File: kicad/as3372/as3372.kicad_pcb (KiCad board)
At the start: 4 copper layers, 80 x 80 mm, 164 parts, among them J1 Conn_01x01, J2 Conn_01x02, J3 Conn_02x20_Odd_Even, Q1 MMBT3904, Q2 MMBT3904, U1 MUX508, U10 TL072, U11 DG442xY, U13 LM4040AIM3-2.5, U15 M24C02-WMN, U17 MUX508, U18 NE5532, U19 L79L05_TO92, U2 MUX508, U3 NE5532, U4 TL074, U5 TL072, U6 TL074, U7 CAT9555YI-T2, U8 AS3372, U9 AD5328

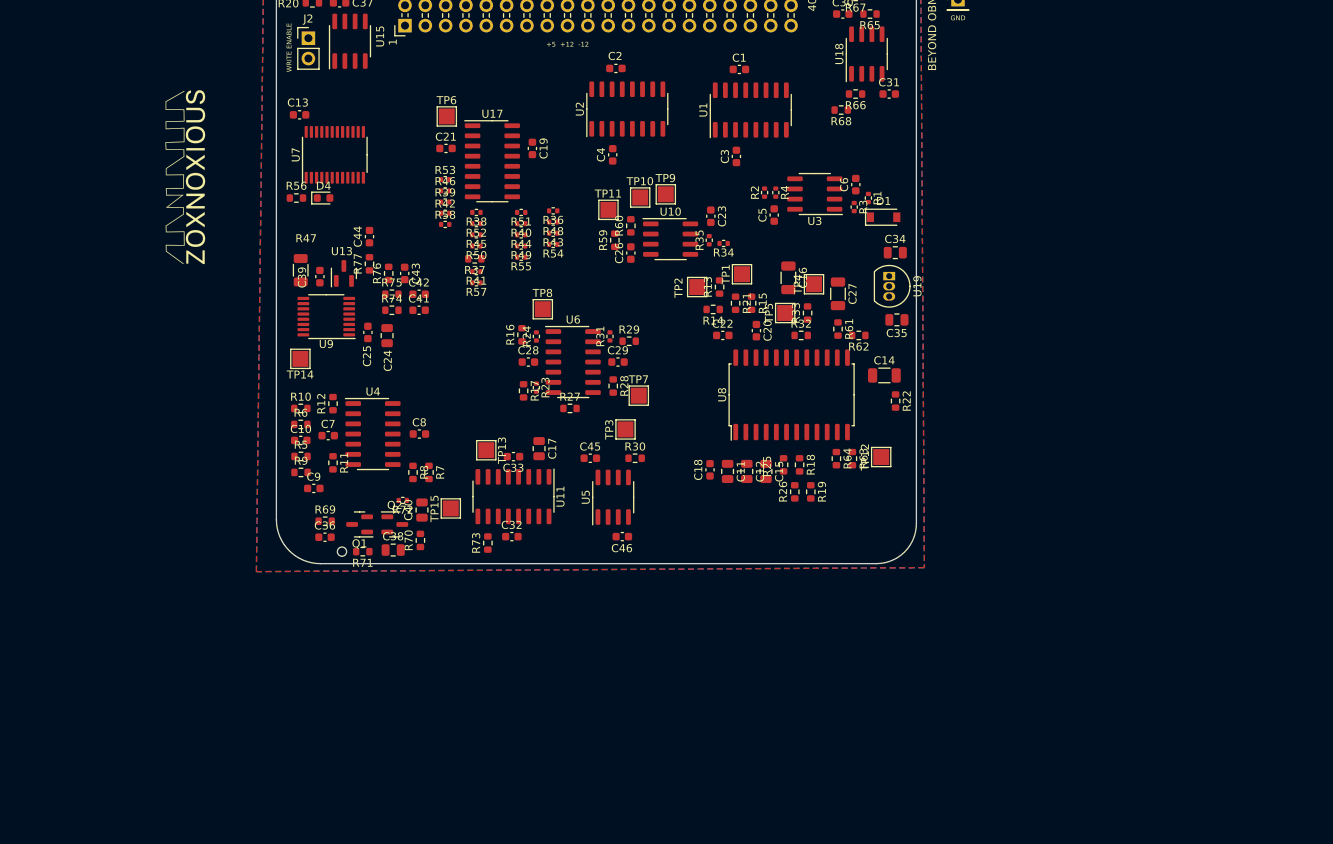
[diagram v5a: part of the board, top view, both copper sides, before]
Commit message: having a tough time routing full filter with modes
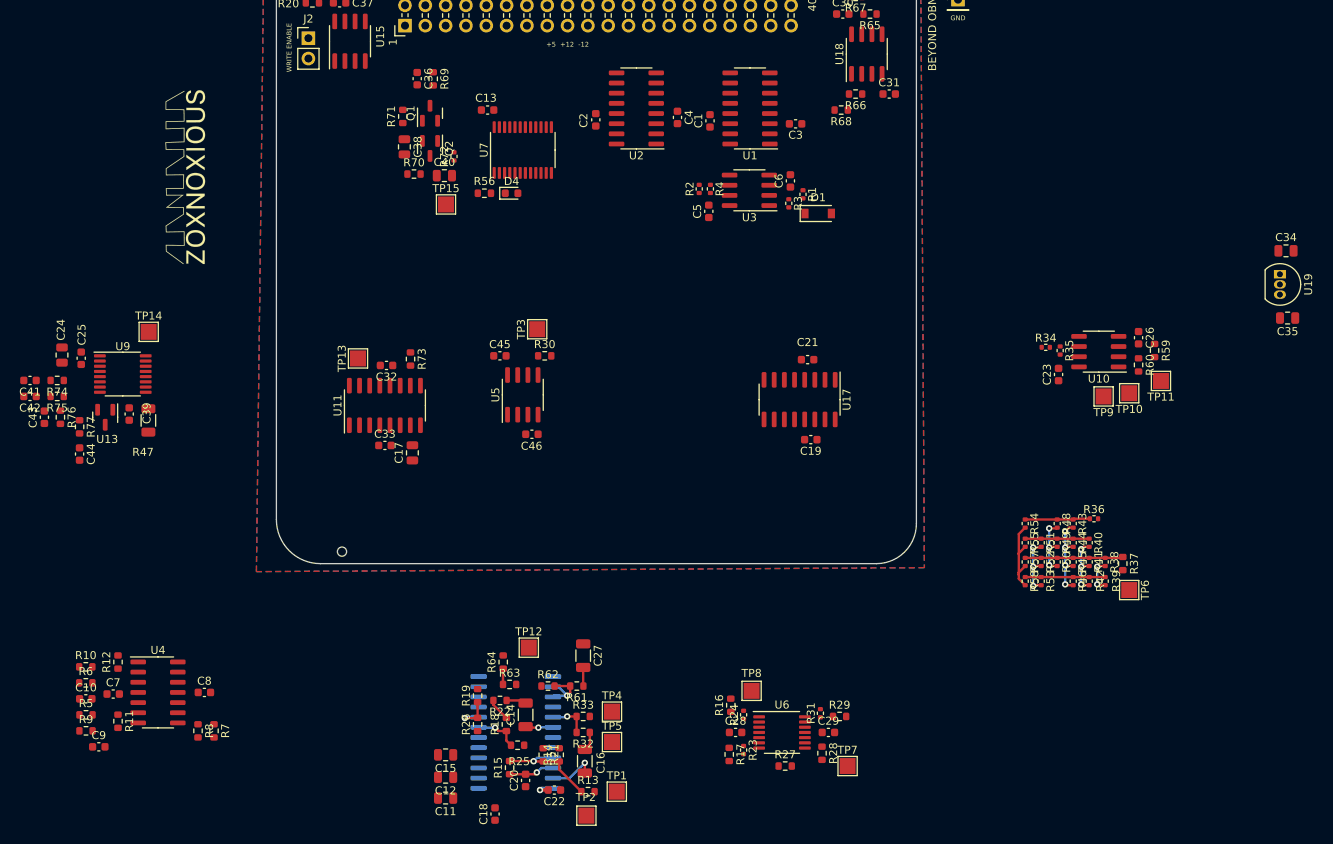
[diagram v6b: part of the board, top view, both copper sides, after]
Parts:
- U6: footprint Package_SO:SOIC-14_3.9x8.7mm_P1.27mm -> Package_SO:TSSOP-14_4.4x5mm_P0.65mm
- U8: moved to B.Cu
- moved TP6 103.8 mm to (173.6, 108.8), turned to -90 degrees
- moved R39 95.1 mm to (170.6, 107.7), turned to -90 degrees
- moved R42 92.7 mm to (168.6, 107.7), turned to -90 degrees
- moved R46 92.4 mm to (166.6, 107.7), turned to -90 degrees
- moved R38 89.9 mm to (170.6, 105.3), turned to -90 degrees
- moved R53 89.8 mm to (162.6, 107.7), turned to -90 degrees
- moved R37 89.5 mm to (172.8, 105.5), turned to -90 degrees
- moved R58 85.1 mm to (160.6, 107.7), turned to -90 degrees
- moved R45 85.1 mm to (166.6, 105.3), turned to -90 degrees
- moved R41 84.8 mm to (168.6, 105.3), turned to -90 degrees
- moved R50 82.6 mm to (164.6, 105.3), turned to -90 degrees
- moved R52 82.3 mm to (162.6, 105.3), turned to -90 degrees
- moved R40 81.4 mm to (168.6, 102.9), turned to -90 degrees
- moved R44 79.0 mm to (166.6, 102.9), turned to -90 degrees
- moved R36 77.8 mm to (169.2, 99.9), turned to 0 degrees
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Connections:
- U1 pad 10: /CARD6_OUT2 -> /CARD1_OUT2
- U1 pad 11: /CARD5_OUT1 -> /CARD2_OUT2
- U1 pad 12: /CARD4_OUT2 -> /CARD3_OUT1
- U1 pad 4: /CARD1_OUT1 -> /CARD7_OUT1
- U1 pad 5: /CARD1_OUT2 -> /CARD6_OUT2
- U1 pad 6: /CARD2_OUT2 -> /CARD5_OUT1
- U1 pad 7: /CARD3_OUT1 -> /CARD4_OUT2
- U1 pad 9: /CARD7_OUT1 -> /CARD1_OUT1
- U11 pad 1: /FILTER_D_CTRL -> /VCF_FM_CTRL
- U11 pad 15: /filter_as3372/VCF_FM -> /filter_as3372/VCA_FM
- U11 pad 16: /VCF_FM_CTRL -> /VCA_FM_CTRL
- U11 pad 2: Net-(C17-Pad2) -> /filter_as3372/VCF_FM
- U11 pad 3: Net-(C18-Pad2) -> Net-(U11-Pad3)
- U11 pad 6: /filter_as3372/VCA_FM -> Net-(C17-Pad2)
- U11 pad 7: Net-(U11-Pad7) -> Net-(C18-Pad2)
- U11 pad 8: /VCA_FM_CTRL -> /FILTER_D_CTRL
- U2 pad 10: /CARD6_OUT1 -> /CARD1_OUT2
- U2 pad 11: /CARD5_OUT2 -> /CARD2_OUT1
- U2 pad 12: /CARD4_OUT1 -> /CARD2_OUT2
- U2 pad 4: /CARD1_OUT2 -> /CARD6_OUT1
- U2 pad 5: /CARD2_OUT1 -> /CARD5_OUT2
- U2 pad 6: /CARD2_OUT2 -> /CARD4_OUT1
- U2 pad 9: /CARD7_OUT1 -> unconnected-(U2-Pad9)
- U5 pad 1: Net-(U11-Pad7) -> Net-(U11-Pad14)
- U5 pad 2: Net-(U11-Pad7) -> Net-(U11-Pad14)
- U5 pad 6: Net-(U11-Pad14) -> Net-(U11-Pad3)
- U5 pad 7: Net-(U11-Pad14) -> Net-(U11-Pad3)
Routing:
- net Net-(R13-Pad1): track 0.00 -> 13.7 mm, vias 0 -> 1
- net /filter_as3372/CELL2_BUFFERED: track 0.00 -> 12.2 mm
- net /filter_as3372/3PHP_OR_3PHP_1PLP: track 0.00 -> 10.9 mm, vias 0 -> 4
- net /filter_as3372/3PAP_OR_3PAP_1PLP: track 0.00 -> 10.5 mm
- net /filter_as3372/CELL1_BUFFERED: track 0.00 -> 10.0 mm
- net /filter_as3372/VCF_OUT_BUFFERED: track 0.00 -> 8.13 mm
- net /filter_as3372/CELL3_BUFFERED: track 0.00 -> 8.00 mm
- net /filter_as3372/2PN_OR_2PN_1PLP: track 0.00 -> 7.91 mm, vias 0 -> 3
- net /filter_as3372/2PHP_1PLP_OR_4PBP: track 0.00 -> 7.72 mm, vias 0 -> 3
- net /filter_as3372/2PHP_OR_2PHP_1PLP: track 0.00 -> 7.60 mm, vias 0 -> 3
- net Net-(R61-Pad2): track 0.00 -> 7.38 mm, vias 0 -> 1
- net Net-(C16-Pad1): track 0.00 -> 6.04 mm, vias 0 -> 1
- net -5V: track 0.00 -> 5.75 mm, vias 0 -> 1
- net Net-(R18-Pad1): track 0.00 -> 5.68 mm, vias 0 -> 1
- net Net-(R19-Pad1): track 0.00 -> 5.33 mm, vias 0 -> 1
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- removed copper zone on In2.Cu, net +5V

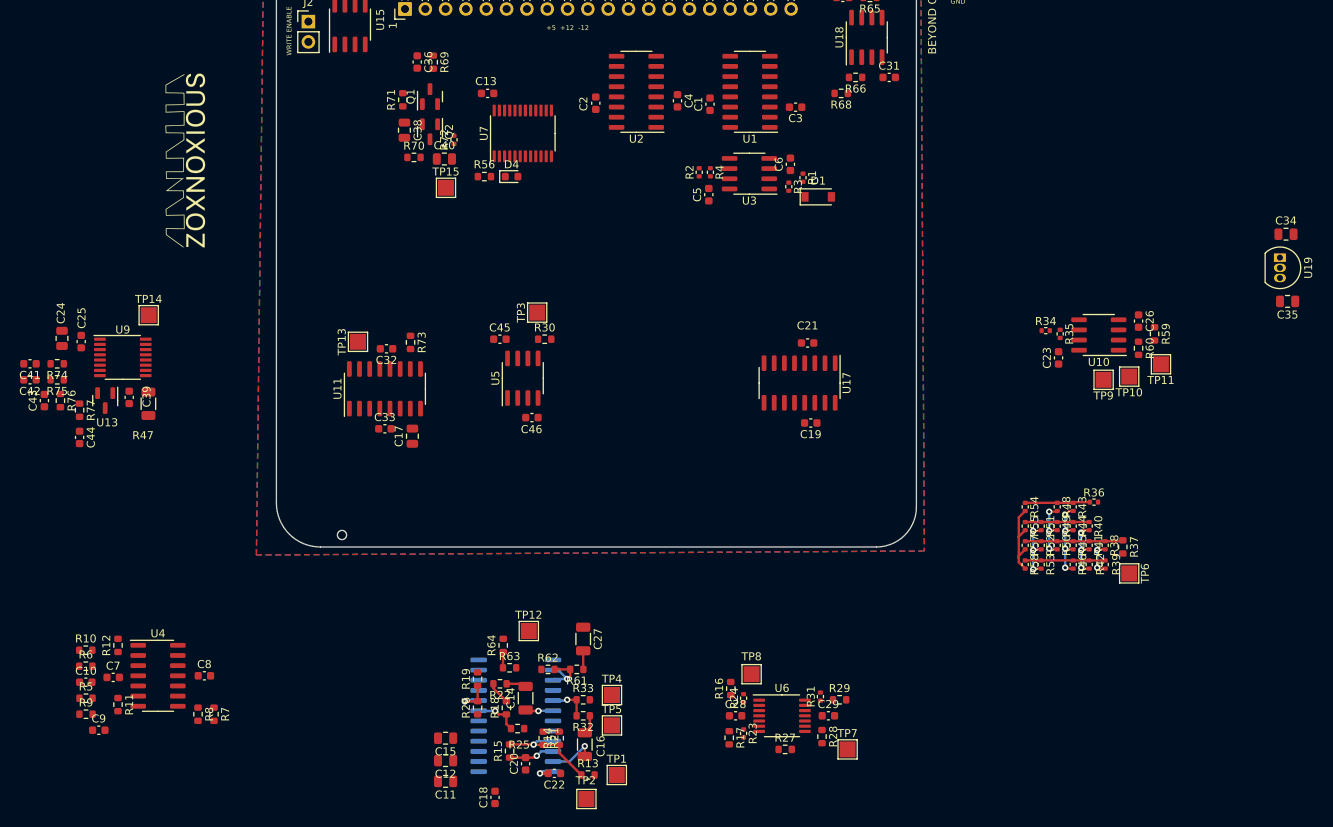
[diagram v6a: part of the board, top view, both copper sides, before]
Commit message: simplify and remove filter mode select
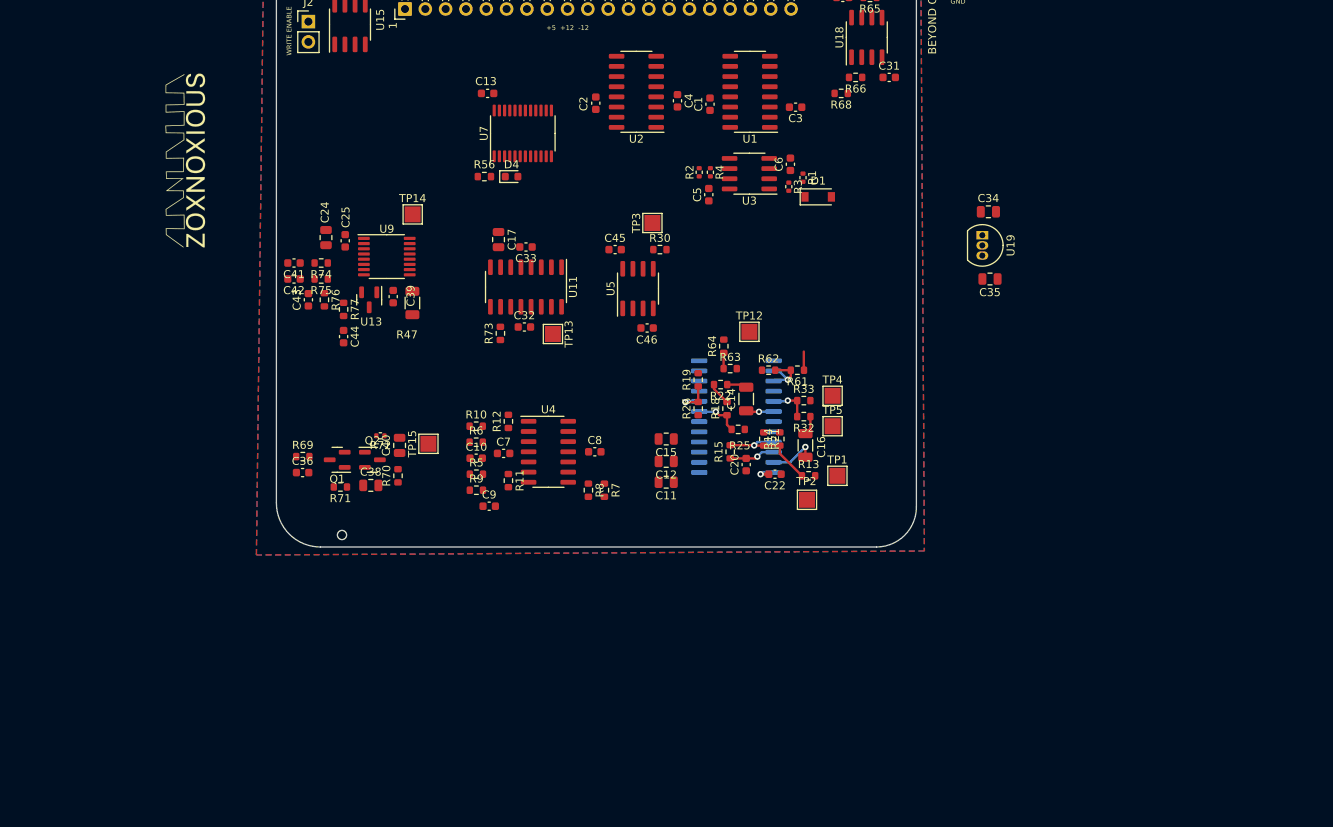
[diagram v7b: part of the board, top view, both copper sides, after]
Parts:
- removed C18: 33p, Capacitor_SMD:C_0603_1608Metric
- removed C19, C21, C23, C26, C28, C29: 0.1u, Capacitor_SMD:C_0603_1608Metric
- removed C27: 2.2u, Capacitor_SMD:C_1206_3216Metric
- removed R16, R17, R29: 1k, Resistor_SMD:R_0603_1608Metric
- removed R23, R24, R31, R34, R35, R38, R39, R40, R42, R43, R46, R48, R50, R53, R58: 100k, Resistor_SMD:R_0402_1005Metric
- removed R27, R28, R59: 10k, Resistor_SMD:R_0603_1608Metric
- removed R36: 56k, Resistor_SMD:R_0402_1005Metric
- removed R37: 62k, Resistor_SMD:R_0603_1608Metric
- removed R41, R49, R51, R52: 49.9k, Resistor_SMD:R_0402_1005Metric
- removed R44, R45, R57: 33.2k, Resistor_SMD:R_0402_1005Metric
- removed R54: 24.9k, Resistor_SMD:R_0402_1005Metric
- removed R55: 16.5k, Resistor_SMD:R_0402_1005Metric
- removed R60: 68k, Resistor_SMD:R_0603_1608Metric
- removed TP10, TP11, TP6, TP7, TP8, TP9: TestPoint, TestPoint:TestPoint_Pad_2.0x2.0mm
- removed U10: TL072, Package_SO:SOIC-8_3.9x4.9mm_P1.27mm
- removed U17: MUX508, Package_SO:SOIC-16_3.9x9.9mm_P1.27mm
- removed U6: TL074, Package_SO:TSSOP-14_4.4x5mm_P0.65mm
- moved C10 56.3 mm to (92.0, 94.4)
- moved C7 56.3 mm to (95.4, 93.8)
- moved C8 56.3 mm to (106.8, 93.6)
- moved C9 56.3 mm to (93.6, 100.4)
- moved R10 56.3 mm to (92.0, 90.4)
- moved R11 56.3 mm to (96.0, 97.2)
- moved R12 56.3 mm to (96.0, 89.8)
- moved R5 56.3 mm to (92.0, 96.4)
- moved R6 56.3 mm to (92.0, 92.4)
- moved R7 56.3 mm to (108.0, 98.4)
- moved R8 56.3 mm to (106.0, 98.4)
- moved R9 56.3 mm to (92.0, 98.4)
- moved U4 56.3 mm to (101.0, 93.6)
- moved C36 53.3 mm to (70.3, 96.2), turned to 0 degrees
- moved R69 51.9 mm to (70.3, 94.2), turned to 0 degrees
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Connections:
- C17 pad 2: Net-(C17-Pad2) -> Net-(U8-Pad1)
- R61 pad 1: Net-(C27-Pad2) -> Net-(C16-Pad2)
- U11 pad 6: Net-(C17-Pad2) -> (no net)
- U11 pad 7: Net-(C18-Pad2) -> (no net)
- U11 pad 8: /FILTER_D_CTRL -> (no net)
- U7 pad 6: /FILTER_A_CTRL -> unconnected-(U7-Pad6)
- U7 pad 7: /FILTER_B_CTRL -> unconnected-(U7-Pad7)
- U7 pad 8: /FILTER_C_CTRL -> unconnected-(U7-Pad8)
- U7 pad 9: /FILTER_D_CTRL -> unconnected-(U7-Pad9)
- U8 pad 1: Net-(C18-Pad2) -> Net-(U8-Pad1)
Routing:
- net /filter_as3372/CELL2_BUFFERED: track 12.2 -> 0.00 mm
- net /filter_as3372/3PHP_OR_3PHP_1PLP: track 10.9 -> 0.00 mm, vias 4 -> 0
- net /filter_as3372/3PAP_OR_3PAP_1PLP: track 10.5 -> 0.00 mm
- net /filter_as3372/CELL1_BUFFERED: track 10.0 -> 0.00 mm
- net /filter_as3372/VCF_OUT_BUFFERED: track 8.13 -> 0.00 mm
- net /filter_as3372/CELL3_BUFFERED: track 8.00 -> 0.00 mm
- net /filter_as3372/2PN_OR_2PN_1PLP: track 7.91 -> 0.00 mm, vias 3 -> 0
- net /filter_as3372/2PHP_1PLP_OR_4PBP: track 7.72 -> 0.00 mm, vias 3 -> 0
- net /filter_as3372/2PHP_OR_2PHP_1PLP: track 7.60 -> 0.00 mm, vias 3 -> 0
- net /filter_as3372/1PLP_OR_2PBP: track 4.28 -> 0.00 mm, vias 2 -> 0
- net Net-(C27-Pad2): track 2.34 -> 0.00 mm
- net Net-(C16-Pad2): track 2.63 -> 4.97 mm

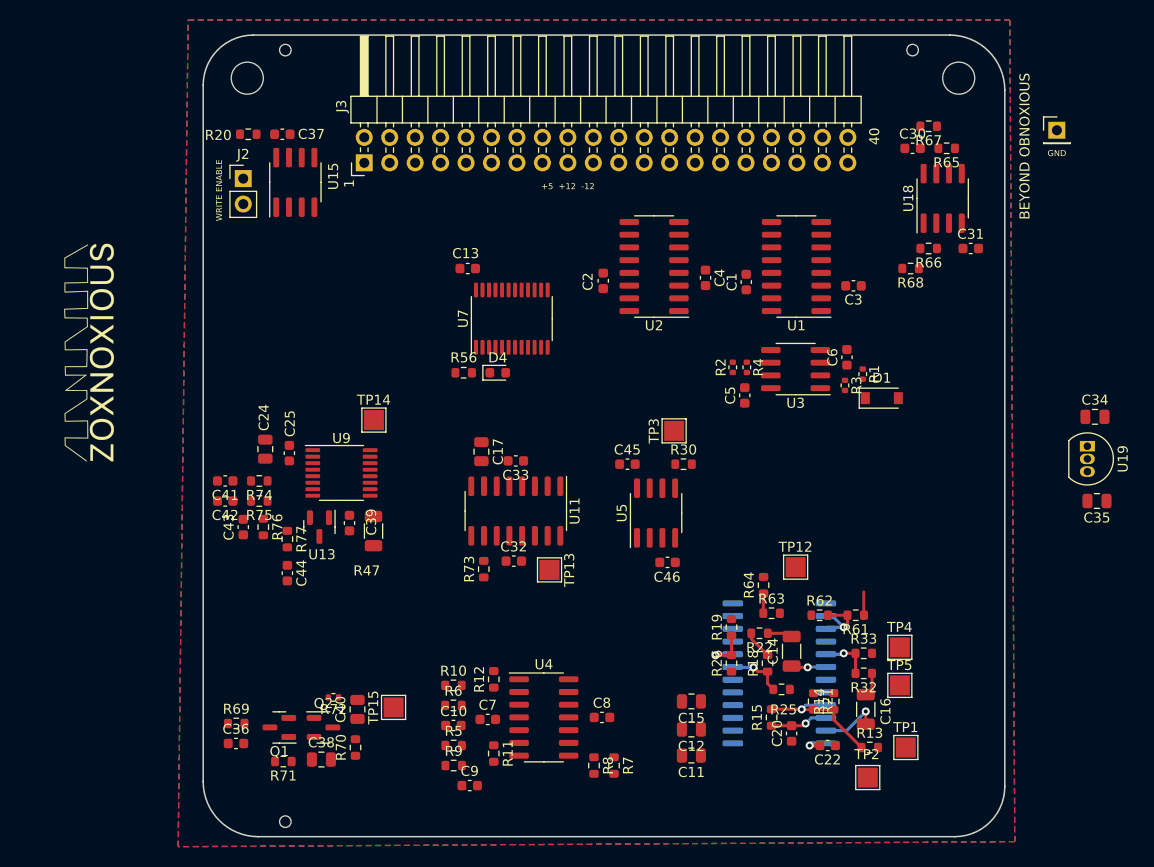
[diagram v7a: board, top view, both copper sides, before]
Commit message: starting routing...which may be detrimental
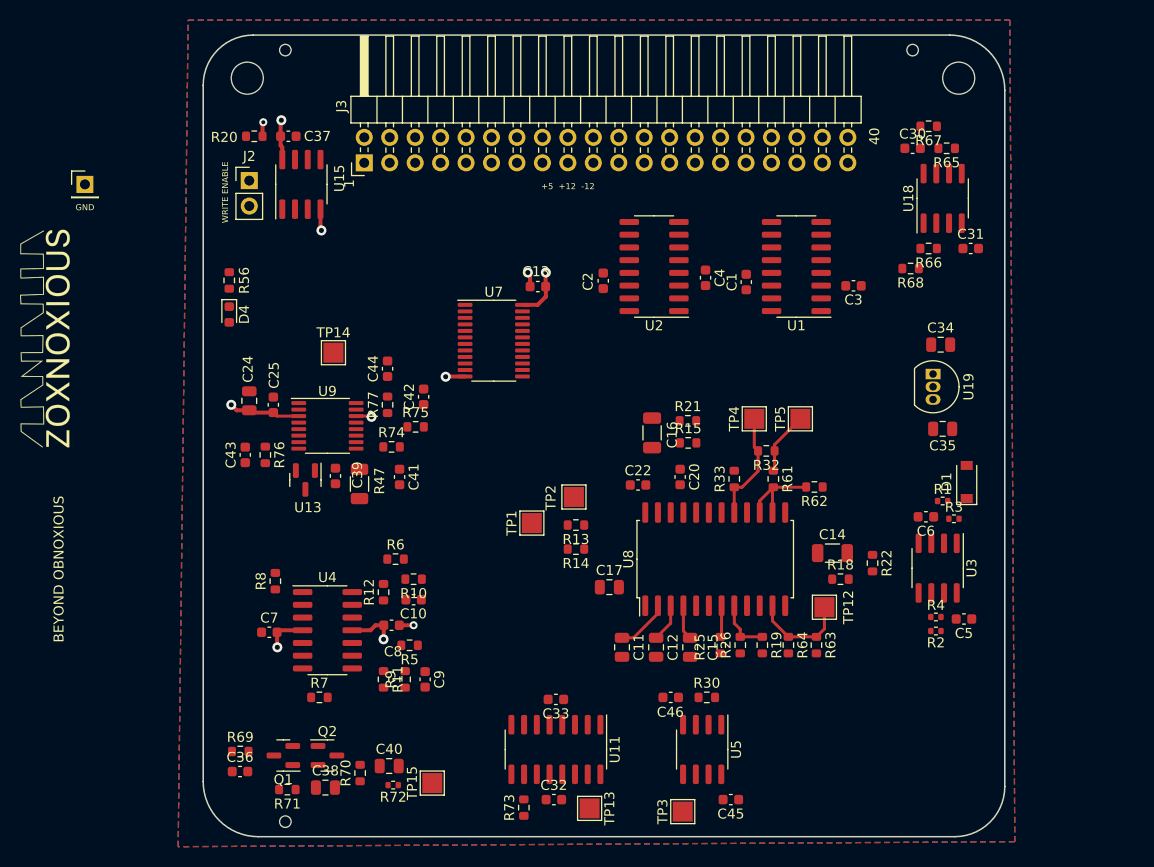
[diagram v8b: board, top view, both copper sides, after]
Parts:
- R61: value 47k -> 22k
- U8: moved to F.Cu
- moved J1 97.2 mm to (55.2, 40.4)
- moved TP1 43.5 mm to (99.8, 74.2), turned to 90 degrees
- moved TP2 40.5 mm to (104.0, 71.6), turned to 90 degrees
- moved TP3 38.0 mm to (114.9, 103.0)
- moved R13 36.8 mm to (104.2, 74.4), turned to 180 degrees
- moved R8 36.7 mm to (74.2, 80.0), turned to 90 degrees
- moved C45 35.0 mm to (119.7, 101.8), turned to 180 degrees
- moved C16 34.9 mm to (111.8, 65.2)
- moved R2 33.2 mm to (140.1, 85.0), turned to 180 degrees
- moved C22 32.2 mm to (110.4, 70.4), turned to 0 degrees
- moved R4 31.3 mm to (140.1, 83.6), turned to 0 degrees
- moved C5 31.2 mm to (142.9, 83.8), turned to 180 degrees
- moved R21 30.7 mm to (115.4, 64.0), turned to 0 degrees
- moved R7 30.2 mm to (78.6, 91.6), turned to 0 degrees
- moved R14 29.9 mm to (104.2, 76.8), turned to 180 degrees
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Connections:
- U11 pad 14: Net-(U11-Pad14) -> /filter_as3372/VCA_FM
- U11 pad 15: /filter_as3372/VCA_FM -> Net-(U11-Pad15)
- U11 pad 2: /filter_as3372/VCF_FM -> Net-(U11-Pad2)
- U11 pad 3: Net-(U11-Pad3) -> /filter_as3372/VCF_FM
- U4 pad 1: /DAC/PAN_VCA_CV -> /DAC/VREF_2.5V_BUFFERED
- U4 pad 10: /DAC/VREF_2.5V -> Net-(C9-Pad1)
- U4 pad 12: GND -> Net-(C10-Pad1)
- U4 pad 13: Net-(U4-Pad13) -> Net-(R12-Pad1)
- U4 pad 14: Net-(U4-Pad13) -> /DAC/PAN_VCA_CV
- U4 pad 2: Net-(R12-Pad1) -> /DAC/VREF_2.5V_BUFFERED
- U4 pad 3: Net-(C10-Pad1) -> /DAC/VREF_2.5V
- U4 pad 5: Net-(C9-Pad1) -> GND
- U4 pad 6: Net-(R11-Pad1) -> Net-(U4-Pad6)
- U4 pad 7: /DAC/VCF_CV -> Net-(U4-Pad6)
- U4 pad 8: /DAC/VREF_2.5V_BUFFERED -> /DAC/VCF_CV
- U4 pad 9: /DAC/VREF_2.5V_BUFFERED -> Net-(R11-Pad1)
- U5 pad 1: Net-(U11-Pad14) -> Net-(U11-Pad2)
- U5 pad 2: Net-(U11-Pad14) -> Net-(U11-Pad2)
- U5 pad 6: Net-(U11-Pad3) -> Net-(U11-Pad15)
- U5 pad 7: Net-(U11-Pad3) -> Net-(U11-Pad15)
- U9 pad 10: /DAC/VCF_CV_DAC -> /DAC/SIG1_VCA_DAC
- U9 pad 11: /DAC/PAN_VCA_CV_DAC -> /DAC/SIG2_VCA_DAC
- U9 pad 12: unconnected-(U9-Pad12) -> /DAC/RESONANCE_DAC
- U9 pad 4: /DAC/SIG1_VCA_DAC -> /DAC/VCF_CV_DAC
- U9 pad 5: /DAC/SIG2_VCA_DAC -> /DAC/PAN_VCA_CV_DAC
- U9 pad 7: /DAC/RESONANCE_DAC -> unconnected-(U9-Pad7)
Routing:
- net +5V: track 0.00 -> 17.8 mm, vias 0 -> 4
- net Net-(R13-Pad1): track 13.7 -> 0.00 mm, vias 1 -> 0
- net GND: track 97.5 -> 106.1 mm, vias 0 -> 5
- net Net-(R63-Pad1): track 1.99 -> 9.85 mm
- net Net-(C16-Pad1): track 6.04 -> 0.00 mm, vias 1 -> 0
- net Net-(R32-Pad2): track 4.99 -> 10.9 mm, vias 1 -> 0
- net -5V: track 5.75 -> 0.00 mm, vias 1 -> 0
- net Net-(C11-Pad1): track 0.00 -> 5.37 mm
- net -12V: track 0.00 -> 4.77 mm, vias 0 -> 1
- net Net-(C12-Pad1): track 0.00 -> 3.80 mm
- net Net-(C14-Pad1): track 3.49 -> 0.00 mm, vias 1 -> 0
- net Net-(C15-Pad1): track 0.00 -> 3.48 mm
- net /VCF_SIGNAL1: track 2.85 -> 0.00 mm
- net Net-(R18-Pad1): track 5.68 -> 3.16 mm, vias 1 -> 0
- net Net-(C14-Pad2): track 2.51 -> 0.00 mm
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- added copper zone on In2.Cu, net +12V
- added copper zone on In2.Cu, net +5V
- added copper zone on In2.Cu, net -12V
